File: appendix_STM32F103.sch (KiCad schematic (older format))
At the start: 27 parts, among them J201 Micro_SD_Card_Det, J202 Conn_02x05_Odd_Even, J204 Conn_ARM_JTAG_SWD_10, SW201 SW_Push, U201 STM32F103ZETx, U202 NTS0104PW-Q100J, X201 SG-210STF

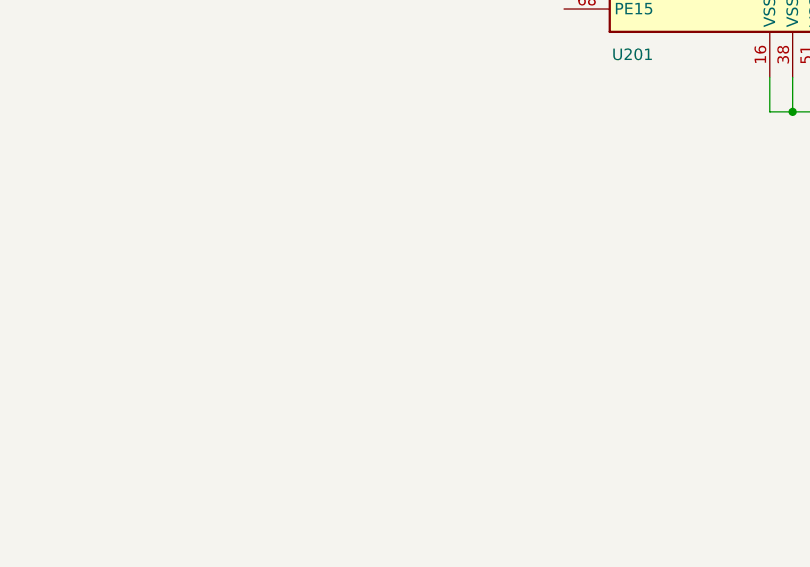
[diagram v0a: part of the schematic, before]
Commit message: added FT2232 by Marco M
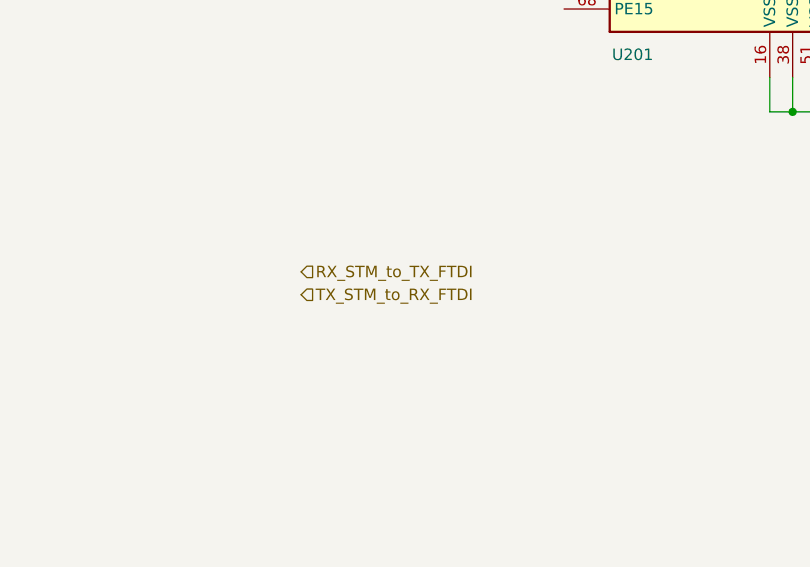
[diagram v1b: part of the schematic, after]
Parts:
- J202: footprint (none) -> Connector_Multicomp:Multicomp_MC9A12-1034_2x05_P2.54mm_Vertical
- U202: footprint (none) -> Housings_SSOP:TSSOP-14_4.4x5mm_Pitch0.65mm
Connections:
- net labels added: RX_STM_to_TX_FTDI, TX_STM_to_RX_FTDI

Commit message: fixed missing symbol issue fixed 3vout cap on FTDI
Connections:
- net labels added: +5V
- net labels removed: 5V
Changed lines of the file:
@@
 Text GLabel 13500 5750 0    50   Input ~ 0
 D_LCD_MOSI
-$Comp
-L SparkFun-PowerSymbols:5V #SUPPLY0201
-U 1 1 5CBB99F0
-P 14650 4800
-F 0 "#SUPPLY0201" H 14700 4800 45  0001 L BNN
-F 1 "5V" V 14650 4928 45  0000 L CNN
-F 2 "XXX-00000" V 14692 4928 60  0001 L CNN
-F 3 "" H 14650 4800 60  0001 C CNN
-	1    14650 4800
-	0    1    1    0
-$EndComp
 Wire Wire Line
 	13700 4800 13900 4800
@@
 F 3 "" H 14150 5650 50  0001 C CNN
 	1    14150 5350
-	1    0    0    -1
-$EndComp
-$Comp
-L SparkFun-PowerSymbols:5V #SUPPLY0202
-U 1 1 5CC5E8C0
-P 14750 5400
-F 0 "#SUPPLY0202" H 14800 5400 45  0001 L BNN
-F 1 "5V" H 14750 5570 45  0000 C CNN
-F 2 "XXX-00000" V 14792 5528 60  0001 L CNN
-F 3 "" H 14750 5400 60  0001 C CNN
-	1    14750 5400
 	1    0    0    -1
 $EndComp
@@
 $EndComp
 $Comp
-L SparkFun-PowerSymbols:5V #SUPPLY0203
-U 1 1 5CD66075
-P 14850 6200
-F 0 "#SUPPLY0203" H 14900 6200 45  0001 L BNN
-F 1 "5V" H 14850 6370 45  0000 C CNN
-F 2 "XXX-00000" V 14892 6328 60  0001 L CNN
-F 3 "" H 14850 6200 60  0001 C CNN
-	1    14850 6200
-	1    0    0    -1
-$EndComp
-$Comp
 L power:GND #PWR0217
 U 1 1 5CD6C32D
@@
 Text HLabel 6950 9750 2    50   Input ~ 0
 TX_STM_to_RX_FTDI
+$Comp
+L power:+5V #PWR04
+U 1 1 5CBEBF25
+P 14850 6200
+F 0 "#PWR04" H 14850 6050 50  0001 C CNN
+F 1 "+5V" H 14865 6373 50  0000 C CNN
+F 2 "" H 14850 6200 50  0001 C CNN
+F 3 "" H 14850 6200 50  0001 C CNN
+	1    14850 6200
+	1    0    0    -1
+$EndComp
+$Comp
+L power:+5V #PWR03
+U 1 1 5CBED41A
+P 14750 5400
+F 0 "#PWR03" H 14750 5250 50  0001 C CNN
+F 1 "+5V" H 14765 5573 50  0000 C CNN
+F 2 "" H 14750 5400 50  0001 C CNN
+F 3 "" H 14750 5400 50  0001 C CNN
+	1    14750 5400
+	1    0    0    -1
+$EndComp
+$Comp
+L power:+5V #PWR02
+U 1 1 5CBEDA11
+P 14650 4800
+F 0 "#PWR02" H 14650 4650 50  0001 C CNN
+F 1 "+5V" V 14665 4928 50  0000 L CNN
+F 2 "" H 14650 4800 50  0001 C CNN
+F 3 "" H 14650 4800 50  0001 C CNN
+	1    14650 4800
+	0    1    1    0
+$EndComp
 $EndSCHEMATC

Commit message: started with STM32 Pinout connections (Mittagspause)
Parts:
- added C203: 10n, Capacitors_SMD:C_0603, symbol Device:C
- added J203: Conn_02x20_Top_Bottom, symbol Connector_Generic:Conn_02x20_Top_Bottom
- added R213, R214, R215, R216: 10k, Resistors_SMD:R_0603, symbol Device:R
- added U203: NTS0104PW-Q100J, Housings_SSOP:TSSOP-14_4.4x5mm_Pitch0.65mm, symbol FHNW-Pro4E-FS19T8-Library:NTS0104PW-Q100J
- R207, R208: value 100k -> 10k
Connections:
- net labels added: +24V, CS_E1, CS_Y, CS_Z1, DIR_E1, DIR_Y, DIR_Z1, E2_ADC_TEMP, E2_CS, E2_EN, E2_END_FIL, E2_FAN1, E2_FAN2, E2_HOTEND, E2_STALL, E2_STEP, E3_CS, EN_E1, EN_Y, EN_Z1, ES_DIR, EXP3_LCD_Beeper, EXP3_LCD_CS, EXP3_LCD_Encoder_A, EXP3_LCD_Encoder_B, EXP3_LCD_Encoder_BTN, EXP3_LCD_MOSI, EXP3_LCD_Reset, EXP3_LCD_SCK, FAN_EXT, MISO, MOSI, SCK, SD_CLK, SD_CMD, SD_DAT0, SD_DAT1, SD_DAT2, SD_DAT3, SD_DETECT, SPI2_MISO, SPI2_MOSI, SPI2_SCK, STALL_E1, STALL_Y, STALL_Z1, STEP_E1, STEP_Y, STEP_Z1, USART1_RX, USART1_TX, USART2_RX, USART2_TX
- net labels removed: Conn_LCD_CS, Conn_LCD_MOSI, Conn_LCD_SCK, D_INT_TMC_STALL_E1, D_INT_TMC_STALL_X, D_INT_TMC_STALL_Y, D_INT_TMC_STALL_Z1, D_LCD_Beeper, D_LCD_CS, D_LCD_Encoder_A, D_LCD_Encoder_B, D_LCD_Encoder_BTN, D_LCD_MOSI, D_LCD_Reset, D_LCD_SCK, D_TMC_CS_E1, D_TMC_CS_X, D_TMC_CS_Y, D_TMC_CS_Z1, D_TMC_DIR_E1, D_TMC_DIR_X, D_TMC_DIR_Y, D_TMC_DIR_Z1, D_TMC_EN_E1, D_TMC_EN_X, D_TMC_EN_Y, D_TMC_EN_Z1, D_TMC_STEP_E1, D_TMC_STEP_X, D_TMC_STEP_Y, D_TMC_STEP_Z1, RX_STM_to_TX_FTDI, TX_STM_to_RX_FTDI
- wire segments 151 -> 259
- no-connect marks 3 -> 28
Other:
- note added: "INT"
- note added: "MISO"
- note added: "MOSI"
- note added: "NSS"
- note added: "RX"
- note added: "SCK"
- note added: "SDIO"
- note added: "SPI2"
- note added: "TODO \nreset review by Dominik"
- note added: "TX"
- note added: "USART1"
- note added: "USART2"
- note added: "double check pinout with footprint!!!"
- note removed: "pull-down on level shift lines ?"
- note removed: "sd detect ?"
- moved on the sheet: J201, J202, J204, R203, R204, R205, R206, R209, R210, R211, R212, U202

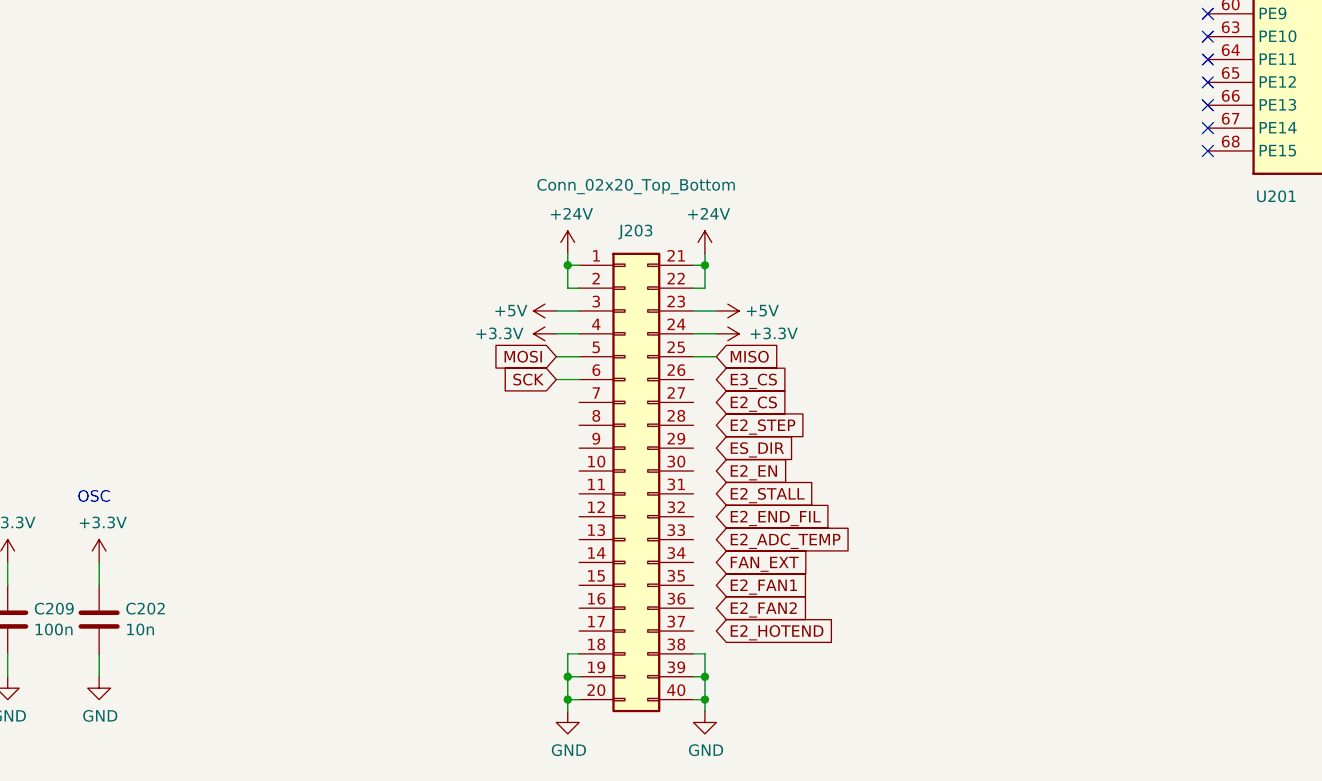
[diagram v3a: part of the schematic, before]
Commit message: layouted FT2232 / SD card
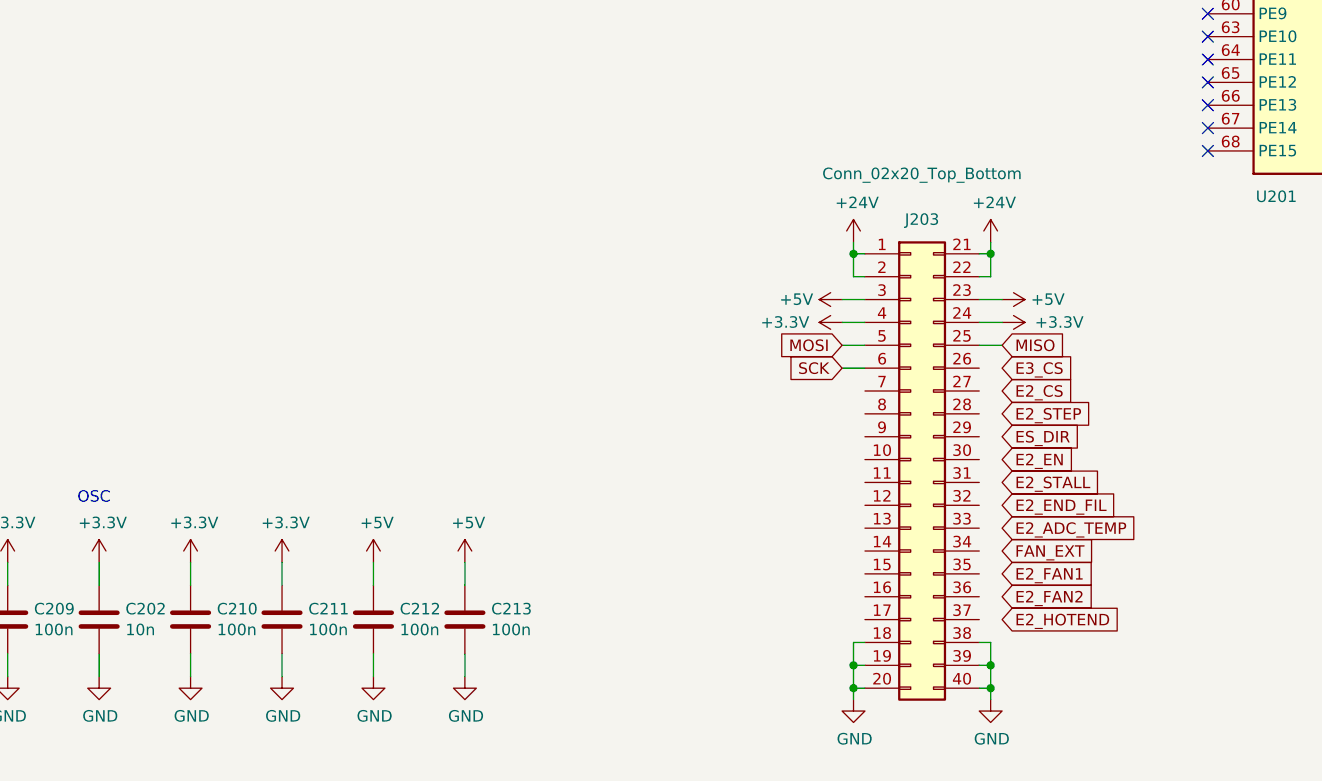
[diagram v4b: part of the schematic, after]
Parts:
- added C210, C211, C212, C213: 100n, Capacitors_SMD:C_0603, symbol Device:C
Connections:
- wire segments 259 -> 267
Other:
- moved on the sheet: J203

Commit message: added cache.lib to git
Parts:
- added R217: 200R, Resistors_SMD:R_0603, symbol Device:R
- J203: footprint (none) -> Connector_PinHeader_2.54mm:PinHeader_2x20_P2.54mm_Vertical
- J204: footprint (none) -> Connector_PinHeader_1.27mm:PinHeader_2x05_P1.27mm_Vertical
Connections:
- net JTAG_RESET: now also R217.2; no longer J204.10 (~RESET~)
- net JTAG_TCK_SWCLK: now also R205.2
- net JTAG_TDI: now also R204.1
- net JTAG_TDO_SWO: now also R206.2
- net JTAG_TMS_SWDIO: now also R203.1
- net at J204.2 (SWDIO/TMS), R210.1: no longer R203.1
- net at J204.8 (NC/TDI), R212.1: no longer R204.1
- net at J204.6 (SWO/TDO), R211.1: no longer R206.2
- net at J204.4 (SWDCLK/TCK), R209.1: no longer R205.2
- new net: J204.10 (~RESET~), R217.1
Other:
- moved on the sheet: R203, R204, R205, R206, R209, R210, R211, R212
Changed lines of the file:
@@
 L Device:R R203
 U 1 1 5CB89A78
-P 14400 8050
-F 0 "R203" V 14300 8100 50  0000 C CNN
-F 1 "10k" V 14400 8050 50  0000 C CNN
-F 2 "Resistors_SMD:R_0603" V 14330 8050 50  0001 C CNN
-F 3 "~" H 14400 8050 50  0001 C CNN
-	1    14400 8050
+P 14800 8050
+F 0 "R203" V 14700 8100 50  0000 C CNN
+F 1 "10k" V 14800 8050 50  0000 C CNN
+F 2 "Resistors_SMD:R_0603" V 14730 8050 50  0001 C CNN
+F 3 "~" H 14800 8050 50  0001 C CNN
+	1    14800 8050
 	-1   0    0    1
 $EndComp
@@
 L Device:R R204
 U 1 1 5CB89E62
-P 14600 8050
-F 0 "R204" V 14500 8100 50  0000 C CNN
-F 1 "10k" V 14600 8050 50  0000 C CNN
-F 2 "Resistors_SMD:R_0603" V 14530 8050 50  0001 C CNN
-F 3 "~" H 14600 8050 50  0001 C CNN
-	1    14600 8050
+P 15000 8050
+F 0 "R204" V 14900 8100 50  0000 C CNN
+F 1 "10k" V 15000 8050 50  0000 C CNN
+F 2 "Resistors_SMD:R_0603" V 14930 8050 50  0001 C CNN
+F 3 "~" H 15000 8050 50  0001 C CNN
+	1    15000 8050
 	-1   0    0    1
 $EndComp
 Wire Wire Line
-	14400 8200 14400 8800
+	14800 8200 14800 8800
 Wire Wire Line
-	14600 8200 14600 9000
+	15000 8200 15000 9000
 Wire Wire Line
-	14600 9000 14800 9000
+	15000 9000 15200 9000
 Wire Wire Line
-	14400 8800 14800 8800
+	14800 8800 15200 8800
 $Comp
 L Device:R R206
 U 1 1 5CBAA3AC
-P 14400 9300
-F 0 "R206" V 14300 9350 50  0000 C CNN
-F 1 "10k" V 14400 9300 50  0000 C CNN
-F 2 "Resistors_SMD:R_0603" V 14330 9300 50  0001 C CNN
-F 3 "~" H 14400 9300 50  0001 C CNN
-	1    14400 9300
+P 14800 9300
+F 0 "R206" V 14700 9350 50  0000 C CNN
+F 1 "10k" V 14800 9300 50  0000 C CNN
+F 2 "Resistors_SMD:R_0603" V 14730 9300 50  0001 C CNN
+F 3 "~" H 14800 9300 50  0001 C CNN
+	1    14800 9300
 	-1   0    0    1
 $EndComp
 Wire Wire Line
-	14400 9150 14400 8900
+	14800 9150 14800 8900
 Wire Wire Line
-	14400 8900 14800 8900
+	14800 8900 15200 8900
 $Comp
 L Device:R R205
 U 1 1 5CBAEA23
-P 14200 9300
-F 0 "R205" V 14100 9350 50  0000 C CNN
-F 1 "10k" V 14200 9300 50  0000 C CNN
-F 2 "Resistors_SMD:R_0603" V 14130 9300 50  0001 C CNN
-F 3 "~" H 14200 9300 50  0001 C CNN
-	1    14200 9300
+P 14600 9300
+F 0 "R205" V 14500 9350 50  0000 C CNN
+F 1 "10k" V 14600 9300 50  0000 C CNN
+F 2 "Resistors_SMD:R_0603" V 14530 9300 50  0001 C CNN
+F 3 "~" H 14600 9300 50  0001 C CNN
+	1    14600 9300
 	-1   0    0    1
 $EndComp
 Wire Wire Line
-	14200 9150 14200 8700
+	14600 9150 14600 8700
 Wire Wire Line
-	14200 8700 14800 8700
+	14600 8700 15200 8700
 $Comp
 L power:GND #PWR0119
 U 1 1 5CBB26E4
-P 14300 9700
-F 0 "#PWR0119" H 14300 9450 50  0001 C CNN
-F 1 "GND" H 14305 9527 50  0000 C CNN
-F 2 "" H 14300 9700 50  0001 C CNN
-F 3 "" H 14300 9700 50  0001 C CNN
-	1    14300 9700
+P 14700 9700
+F 0 "#PWR0119" H 14700 9450 50  0001 C CNN
+F 1 "GND" H 14705 9527 50  0000 C CNN
+F 2 "" H 14700 9700 50  0001 C CNN
+F 3 "" H 14700 9700 50  0001 C CNN
+	1    14700 9700
 	1    0    0    -1
 $EndComp
 Wire Wire Line
-	14200 9450 14200 9600
+	14600 9450 14600 9600
 Wire Wire Line
-	14200 9600 14300 9600
+	14600 9600 14700 9600
 Wire Wire Line
-	14400 9600 14400 9450
+	14800 9600 14800 9450
 Wire Wire Line
-	14300 9600 14300 9700
-Connection ~ 14300 9600
+	14700 9600 14700 9700
+Connection ~ 14700 9600
 Wire Wire Line
-	14300 9600 14400 9600
+	14700 9600 14800 9600
 $Comp
 L power:+3.3V #PWR0120
 U 1 1 5CBBABAF
-P 14400 7800
-F 0 "#PWR0120" H 14400 7650 50  0001 C CNN
-F 1 "+3.3V" H 14415 7973 50  0000 C CNN
-F 2 "" H 14400 7800 50  0001 C CNN
-F 3 "" H 14400 7800 50  0001 C CNN
-	1    14400 7800
+P 14800 7800
+F 0 "#PWR0120" H 14800 7650 50  0001 C CNN
+F 1 "+3.3V" H 14815 7973 50  0000 C CNN
+F 2 "" H 14800 7800 50  0001 C CNN
+F 3 "" H 14800 7800 50  0001 C CNN
+	1    14800 7800
 	1    0    0    -1
 $EndComp
 Wire Wire Line
-	14600 7900 14600 7850
+	15000 7900 15000 7850
 Wire Wire Line
-	14600 7850 14400 7850
+	15000 7850 14800 7850
 Wire Wire Line
-	14400 7900 14400 7850
-Connection ~ 14400 7850
+	14800 7900 14800 7850
+Connection ~ 14800 7850
 Wire Wire Line
-	14400 7850 14400 7800
+	14800 7850 14800 7800
 $Comp
 L power:+3.3VA #PWR0123
@@
 F 0 "J204" H 13700 9350 50  0000 R CNN
 F 1 "Conn_ARM_JTAG_SWD_10" V 12900 9250 50  0000 R CNN
-F 2 "" H 13350 8800 50  0001 C CNN
+F 2 "Connector_PinHeader_1.27mm:PinHeader_2x05_P1.27mm_Vertical" H 13350 8800 50  0001 C CNN
 F 3 "http://infocenter.arm.com/help/topic/com.arm.doc.ddi0314h/DDI0314H_coresight_components_trm.pdf" V 13000 7550 50  0001 C CNN
 	1    13350 8800
@@
 Wire Wire Line
 	13350 9450 13350 9400
-Wire Wire Line
-	13850 8500 13900 8500
-Text GLabel 13900 8500 2    50   Input ~ 0
+Text GLabel 15200 8500 2    50   Input ~ 0
 JTAG_RESET
 $Comp
@@
 Wire Wire Line
 	14850 5000 14650 5000
-Wire Wire Line
-	13850 8700 14200 8700
-Connection ~ 14200 8700
-Wire Wire Line
-	14400 8800 13850 8800
-Connection ~ 14400 8800
-Wire Wire Line
-	13850 8900 14400 8900
-Connection ~ 14400 8900
-Wire Wire Line
-	14600 9000 13850 9000
-Connection ~ 14600 9000
 $Comp
 L Device:R R212
 U 1 1 5CD04150
-P 14950 9000
-F 0 "R212" V 15350 9050 50  0000 C CNN
-F 1 "200R" V 14950 9000 50  0000 C CNN
-F 2 "Resistors_SMD:R_0603" V 14880 9000 50  0001 C CNN
-F 3 "~" H 14950 9000 50  0001 C CNN
-	1    14950 9000
+P 14100 9000
+F 0 "R212" V 13700 9000 50  0000 C CNN
+F 1 "200R" V 14100 9000 50  0000 C CNN
+F 2 "Resistors_SMD:R_0603" V 14030 9000 50  0001 C CNN
+F 3 "~" H 14100 9000 50  0001 C CNN
+	1    14100 9000
 	0    -1   -1   0
 $EndComp
@@
 L Device:R R211
 U 1 1 5CD05002
-P 14950 8900
-F 0 "R211" V 15350 8950 50  0000 C CNN
-F 1 "200R" V 14950 8900 50  0000 C CNN
-F 2 "Resistors_SMD:R_0603" V 14880 8900 50  0001 C CNN
-F 3 "~" H 14950 8900 50  0001 C CNN
-	1    14950 8900
+P 14100 8900
+F 0 "R211" V 13700 8900 50  0000 C CNN
+F 1 "200R" V 14100 8900 50  0000 C CNN
+F 2 "Resistors_SMD:R_0603" V 14030 8900 50  0001 C CNN
+F 3 "~" H 14100 8900 50  0001 C CNN
+	1    14100 8900
 	0    -1   -1   0
 $EndComp
@@
 L Device:R R210
 U 1 1 5CD0523F
-P 14950 8800
-F 0 "R210" V 15350 8850 50  0000 C CNN
-F 1 "200R" V 14950 8800 50  0000 C CNN
-F 2 "Resistors_SMD:R_0603" V 14880 8800 50  0001 C CNN
-F 3 "~" H 14950 8800 50  0001 C CNN
-	1    14950 8800
+P 14100 8800
+F 0 "R210" V 13700 8800 50  0000 C CNN
+F 1 "200R" V 14100 8800 50  0000 C CNN
+F 2 "Resistors_SMD:R_0603" V 14030 8800 50  0001 C CNN
+F 3 "~" H 14100 8800 50  0001 C CNN
+	1    14100 8800
 	0    -1   -1   0
 $EndComp
@@
 L Device:R R209
 U 1 1 5CD053EB
-P 14950 8700
-F 0 "R209" V 15350 8750 50  0000 C CNN
-F 1 "200R" V 14950 8700 50  0000 C CNN
-F 2 "Resistors_SMD:R_0603" V 14880 8700 50  0001 C CNN
-F 3 "~" H 14950 8700 50  0001 C CNN
-	1    14950 8700
+P 14100 8700
+F 0 "R209" V 13700 8700 50  0000 C CNN
+F 1 "200R" V 14100 8700 50  0000 C CNN
+F 2 "Resistors_SMD:R_0603" V 14030 8700 50  0001 C CNN
+F 3 "~" H 14100 8700 50  0001 C CNN
+	1    14100 8700
 	0    -1   -1   0
 $EndComp
 Wire Wire Line
-	15100 8700 15200 8700
-Wire Wire Line
-	15100 8800 15200 8800
-Wire Wire Line
-	15100 8900 15200 8900
-Wire Wire Line
-	15100 9000 15200 9000
-Wire Wire Line
 	14550 3950 14300 3950
 Wire Wire Line
@@
 F 0 "J203" H 6850 10900 50  0000 C CNN
 F 1 "Conn_02x20_Top_Bottom" H 6850 11100 50  0000 C CNN
-F 2 "" H 6800 9850 50  0001 C CNN
+F 2 "Connector_PinHeader_2.54mm:PinHeader_2x20_P2.54mm_Vertical" H 6800 9850 50  0001 C CNN
 F 3 "~" H 6800 9850 50  0001 C CNN
 	1    6800 9850
@@
 	1    0    0    -1
 $EndComp
+Wire Wire Line
+	13850 8700 13950 8700
+Wire Wire Line
+	13850 8800 13950 8800
+Wire Wire Line
+	13950 8900 13850 8900
+Wire Wire Line
+	13850 9000 13950 9000
+Wire Wire Line
+	14250 8700 14600 8700
+Connection ~ 14600 8700
+Wire Wire Line
+	14800 8800 14250 8800
+Connection ~ 14800 8800
+Wire Wire Line
+	14250 8900 14800 8900
+Connection ~ 14800 8900
+Wire Wire Line
+	15000 9000 14250 9000
+Connection ~ 15000 9000
+$Comp
+L Device:R R217
+U 1 1 5CDCD7F7
+P 14100 8500
+F 0 "R217" V 14200 8550 50  0000 C CNN
+F 1 "200R" V 14100 8500 50  0000 C CNN
+F 2 "Resistors_SMD:R_0603" V 14030 8500 50  0001 C CNN
+F 3 "~" H 14100 8500 50  0001 C CNN
+	1    14100 8500
+	0    -1   -1   0
+$EndComp
+Wire Wire Line
+	13850 8500 13950 8500
+Wire Wire Line
+	14250 8500 15200 8500
 $EndSCHEMATC

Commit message: cleaned up Layout
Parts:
- removed R202: 100k, Resistors_SMD:R_0603, symbol Device:R
- added D?: LED, LED_SMD:LED_0805_2012Metric, symbol Device:LED
- added R?: 330R, Resistors_SMD:R_0603, symbol Device:R
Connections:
- new net: D?.2 (A), R?.2
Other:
- note removed: "pull-up for #EN"
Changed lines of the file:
@@
 RCC_OSC_IN
-$Comp
-L Device:R R202
-U 1 1 5CB9810D
-P 2400 3500
-F 0 "R202" H 2470 3546 50  0000 L CNN
-F 1 "100k" H 2470 3455 50  0000 L CNN
-F 2 "Resistors_SMD:R_0603" V 2330 3500 50  0001 C CNN
-F 3 "~" H 2400 3500 50  0001 C CNN
-	1    2400 3500
-	1    0    0    -1
-$EndComp
-Text Notes 1600 3400 0    50   ~ 0
-pull-up for #EN
 $Comp
 L power:GND #PWR0212
@@
 Wire Wire Line
 	14250 8500 15200 8500
+$Comp
+L Device:R R?
+U 1 1 5CDABFCE
+P 3350 4400
+F 0 "R?" H 3420 4446 50  0000 L CNN
+F 1 "330R" H 3420 4355 50  0000 L CNN
+F 2 "Resistors_SMD:R_0603" V 3280 4400 50  0001 C CNN
+F 3 "~" H 3350 4400 50  0001 C CNN
+	1    3350 4400
+	1    0    0    -1
+$EndComp
+$Comp
+L Device:LED D?
+U 1 1 5CDABFD4
+P 3350 4800
+F 0 "D?" V 3389 4683 50  0000 R CNN
+F 1 "LED" V 3298 4683 50  0000 R CNN
+F 2 "LED_SMD:LED_0805_2012Metric" H 3350 4800 50  0001 C CNN
+F 3 "~" H 3350 4800 50  0001 C CNN
+	1    3350 4800
+	0    -1   -1   0
+$EndComp
+Wire Wire Line
+	3350 4550 3350 4650
 $EndSCHEMATC

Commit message: Layout update
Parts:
- removed J203: Conn_02x20_Top_Bottom, Connector_PinHeader_2.54mm:PinHeader_2x20_P2.54mm_Vertical, symbol Connector_Generic:Conn_02x20_Top_Bottom
- added J203: Conn_02x20_Odd_Even, Connector_PinHeader_2.54mm:PinHeader_2x20_P2.54mm_Vertical, symbol Connector_Generic:Conn_02x20_Odd_Even
- gave numbers to parts that had none: 2
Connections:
- net +24V: now also J203.1 (Pin_1), J203.2 (Pin_2), J203.3 (Pin_3), J203.4 (Pin_4)
- net +3V3: now also J203.7 (Pin_7), J203.8 (Pin_8)
- net +5V: now also J203.5 (Pin_5), J203.6 (Pin_6)
- net GND: now also J203.35 (Pin_35), J203.36 (Pin_36), J203.37 (Pin_37), J203.38 (Pin_38), J203.39 (Pin_39), J203.40 (Pin_40)
- net MISO: now also J203.10 (Pin_10)
- net MOSI: now also J203.9 (Pin_9)
- net SCK: now also J203.11 (Pin_11)
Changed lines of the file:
@@
-$EndComp
-$Comp
-L Connector_Generic:Conn_02x20_Top_Bottom J203
-U 1 1 5CC80F37
-P 6800 9850
-F 0 "J203" H 6850 10900 50  0000 C CNN
-F 1 "Conn_02x20_Top_Bottom" H 6850 11100 50  0000 C CNN
-F 2 "Connector_PinHeader_2.54mm:PinHeader_2x20_P2.54mm_Vertical" H 6800 9850 50  0001 C CNN
-F 3 "~" H 6800 9850 50  0001 C CNN
-	1    6800 9850
-	1    0    0    -1
 $EndComp
 $Comp
@@
 	14250 8500 15200 8500
 $Comp
-L Device:R R?
+L Device:R R202
 U 1 1 5CDABFCE
 P 3350 4400
-F 0 "R?" H 3420 4446 50  0000 L CNN
+F 0 "R202" H 3420 4446 50  0000 L CNN
 F 1 "330R" H 3420 4355 50  0000 L CNN
 F 2 "Resistors_SMD:R_0603" V 3280 4400 50  0001 C CNN
@@
 $EndComp
 $Comp
-L Device:LED D?
+L Device:LED D201
 U 1 1 5CDABFD4
 P 3350 4800
-F 0 "D?" V 3389 4683 50  0000 R CNN
+F 0 "D201" V 3389 4683 50  0000 R CNN
 F 1 "LED" V 3298 4683 50  0000 R CNN
 F 2 "LED_SMD:LED_0805_2012Metric" H 3350 4800 50  0001 C CNN
@@
 Wire Wire Line
 	3350 4550 3350 4650
+$Comp
+L Connector_Generic:Conn_02x20_Odd_Even J203
+U 1 1 5CCA330B
+P 6800 9850
+F 0 "J203" H 6850 11200 50  0000 C CNN
+F 1 "Conn_02x20_Odd_Even" H 6850 11100 50  0000 C CNN
+F 2 "Connector_PinHeader_2.54mm:PinHeader_2x20_P2.54mm_Vertical" H 6800 9850 50  0001 C CNN
+F 3 "~" H 6800 9850 50  0001 C CNN
+	1    6800 9850
+	1    0    0    -1
+$EndComp
 $EndSCHEMATC
